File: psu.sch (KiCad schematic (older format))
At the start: 13 parts, among them P1 CONN_01X03, U5 LM7812CT, U6 LM7912CT

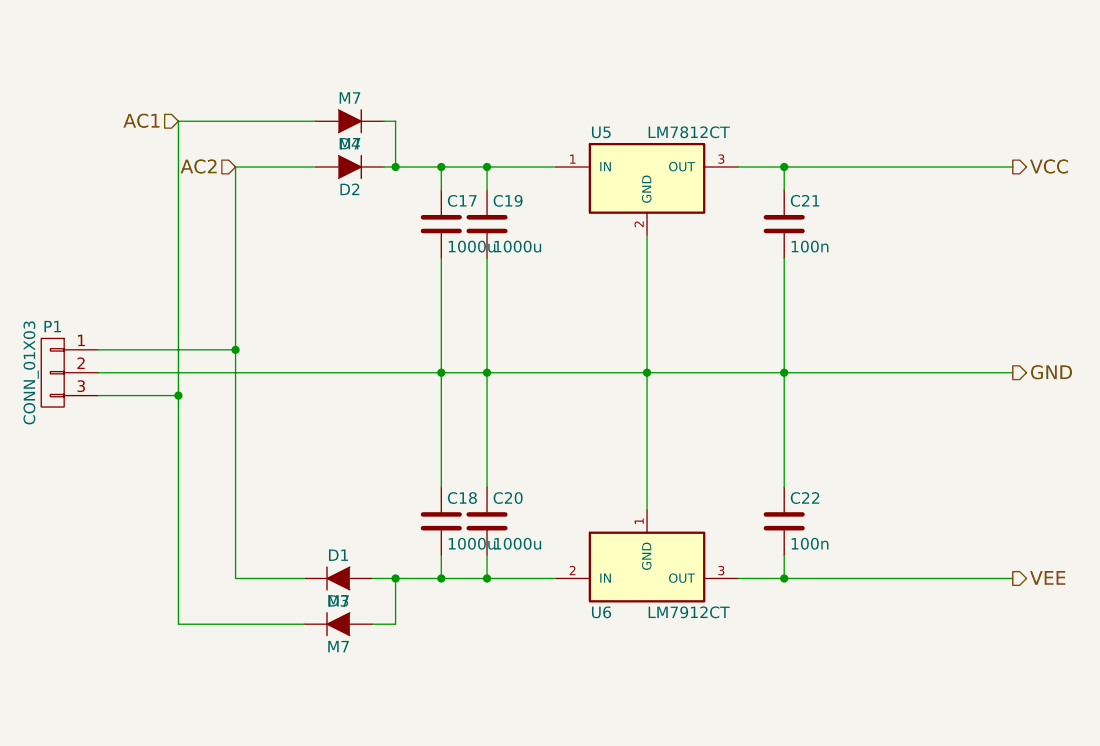
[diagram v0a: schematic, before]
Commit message: added reverse protection diodes to regulators, bumped to Rev.B
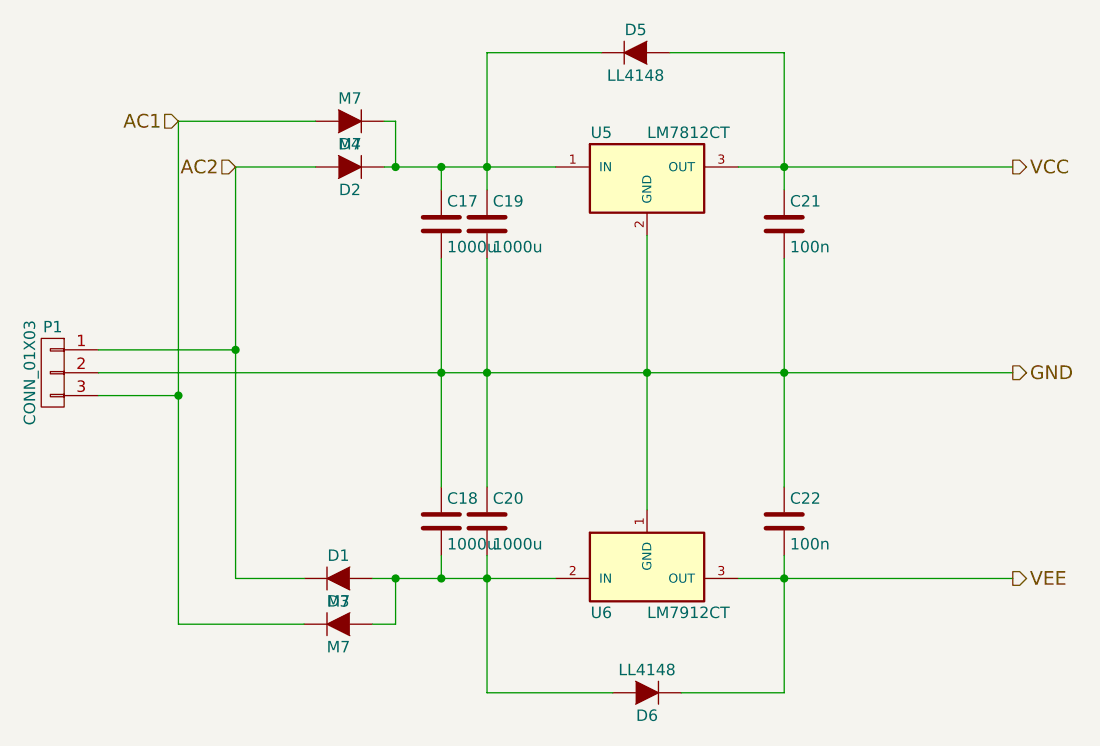
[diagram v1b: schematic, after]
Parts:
- added D5, D6: LL4148, Diodes_SMD:D_MiniMELF, symbol D
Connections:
- net VCC: now also D5.2 (A)
- net VEE: now also D6.1 (K)
- net at C18.2, C20.2, D1.2 (A)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: now also D6.2 (A)
- net at C17.1, C19.1, D2.1 (K)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: now also D5.1 (K)
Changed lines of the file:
@@
 Sheet 3 3
 Title "appnote-amplifier regulated power supply"
-Date "2017-10-28"
-Rev "A"
+Date "2017-12-27"
+Rev "B"
 Comp ""
 Comment1 ""
@@
 Connection ~ 4600 3200
 Wire Wire Line
-	4800 3200 4800 3300
+	4800 2700 4800 3300
 Connection ~ 4800 3200
 Wire Wire Line
@@
 	5900 3200 7100 3200
 Wire Wire Line
-	6100 3200 6100 3300
+	6100 2700 6100 3300
 Wire Wire Line
 	6100 3600 6100 4600
@@
 Connection ~ 4600 5000
 Wire Wire Line
-	4800 5000 4800 4900
+	4800 4900 4800 5500
 Connection ~ 4800 5000
 $Comp
@@
 	5900 5000 7100 5000
 Wire Wire Line
-	6100 5000 6100 4900
+	6100 4900 6100 5500
 Connection ~ 6100 5000
 $Comp
@@
 Text HLabel 3700 3200 0    60   Input ~ 0
 AC2
+$Comp
+L D D5
+U 1 1 5A4380AA
+P 5450 2700
+F 0 "D5" H 5450 2800 50  0000 C CNN
+F 1 "LL4148" H 5450 2600 50  0000 C CNN
+F 2 "Diodes_SMD:D_MiniMELF" H 5450 2700 50  0001 C CNN
+F 3 "" H 5450 2700 50  0000 C CNN
+	1    5450 2700
+	1    0    0    -1
+$EndComp
+$Comp
+L D D6
+U 1 1 5A4382E8
+P 5500 5500
+F 0 "D6" H 5500 5600 50  0000 C CNN
+F 1 "LL4148" H 5500 5400 50  0000 C CNN
+F 2 "Diodes_SMD:D_MiniMELF" H 5500 5500 50  0001 C CNN
+F 3 "" H 5500 5500 50  0000 C CNN
+	1    5500 5500
+	-1   0    0    1
+$EndComp
+Wire Wire Line
+	5300 2700 4800 2700
+Wire Wire Line
+	5600 2700 6100 2700
+Wire Wire Line
+	4800 5500 5350 5500
+Wire Wire Line
+	6100 5500 5650 5500
 $EndSCHEMATC

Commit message: shrunk power connector, made all diodes same type, mentioned 5+5V operation in errata
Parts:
- D5, D6: value LL4148 -> M7; footprint Diodes_SMD:D_MiniMELF -> Diodes_SMD:D_SMA
- P1: footprint Terminal_Blocks:TerminalBlock_Pheonix_MKDS1.5-3pol -> Terminals_Phoenix:TerminalBlock_Phoenix_MPT-2.54mm_3pol
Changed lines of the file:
@@
 F 0 "P1" H 2900 4300 50  0000 C CNN
 F 1 "CONN_01X03" V 3000 4100 50  0000 C CNN
-F 2 "Terminal_Blocks:TerminalBlock_Pheonix_MKDS1.5-3pol" H 2900 4100 50  0001 C CNN
+F 2 "Terminals_Phoenix:TerminalBlock_Phoenix_MPT-2.54mm_3pol" H 2900 4100 50  0001 C CNN
 F 3 "" H 2900 4100 50  0000 C CNN
 	1    2900 4100
@@
 Text HLabel 3700 3200 0    60   Input ~ 0
 AC2
-$Comp
-L D D5
-U 1 1 5A4380AA
-P 5450 2700
-F 0 "D5" H 5450 2800 50  0000 C CNN
-F 1 "LL4148" H 5450 2600 50  0000 C CNN
-F 2 "Diodes_SMD:D_MiniMELF" H 5450 2700 50  0001 C CNN
-F 3 "" H 5450 2700 50  0000 C CNN
-	1    5450 2700
-	1    0    0    -1
-$EndComp
-$Comp
-L D D6
-U 1 1 5A4382E8
-P 5500 5500
-F 0 "D6" H 5500 5600 50  0000 C CNN
-F 1 "LL4148" H 5500 5400 50  0000 C CNN
-F 2 "Diodes_SMD:D_MiniMELF" H 5500 5500 50  0001 C CNN
-F 3 "" H 5500 5500 50  0000 C CNN
-	1    5500 5500
-	-1   0    0    1
-$EndComp
 Wire Wire Line
 	5300 2700 4800 2700
@@
 Wire Wire Line
 	6100 5500 5650 5500
+$Comp
+L D D5
+U 1 1 5A43A934
+P 5450 2700
+F 0 "D5" H 5450 2800 50  0000 C CNN
+F 1 "M7" H 5450 2600 50  0000 C CNN
+F 2 "Diodes_SMD:D_SMA" H 5450 2700 50  0001 C CNN
+F 3 "" H 5450 2700 50  0000 C CNN
+	1    5450 2700
+	1    0    0    -1
+$EndComp
+$Comp
+L D D6
+U 1 1 5A43A9BC
+P 5500 5500
+F 0 "D6" H 5500 5600 50  0000 C CNN
+F 1 "M7" H 5500 5400 50  0000 C CNN
+F 2 "Diodes_SMD:D_SMA" H 5500 5500 50  0001 C CNN
+F 3 "" H 5500 5500 50  0000 C CNN
+	1    5500 5500
+	-1   0    0    1
+$EndComp
 $EndSCHEMATC
